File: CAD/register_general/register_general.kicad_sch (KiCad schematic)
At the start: 29 parts, among them J1 Conn_01x16_Pin, J2 Conn_01x16_Pin, J3 load select, J4 output select, U1 74HC245, U2 74HC377

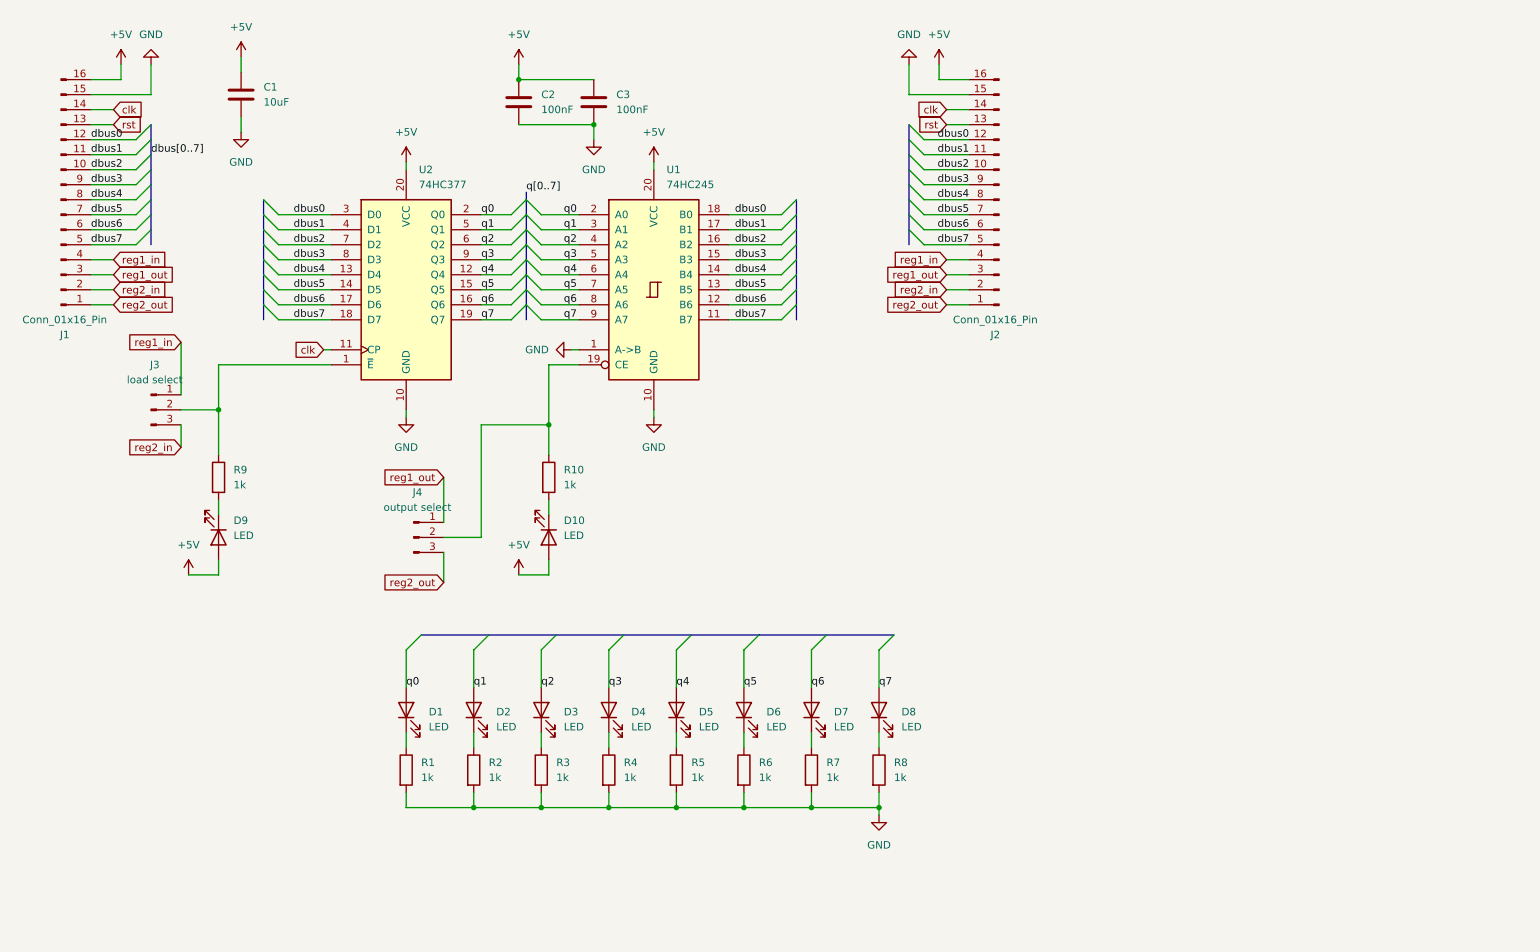
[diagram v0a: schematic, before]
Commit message: add NetClasses, TestPads, remove jumper pins
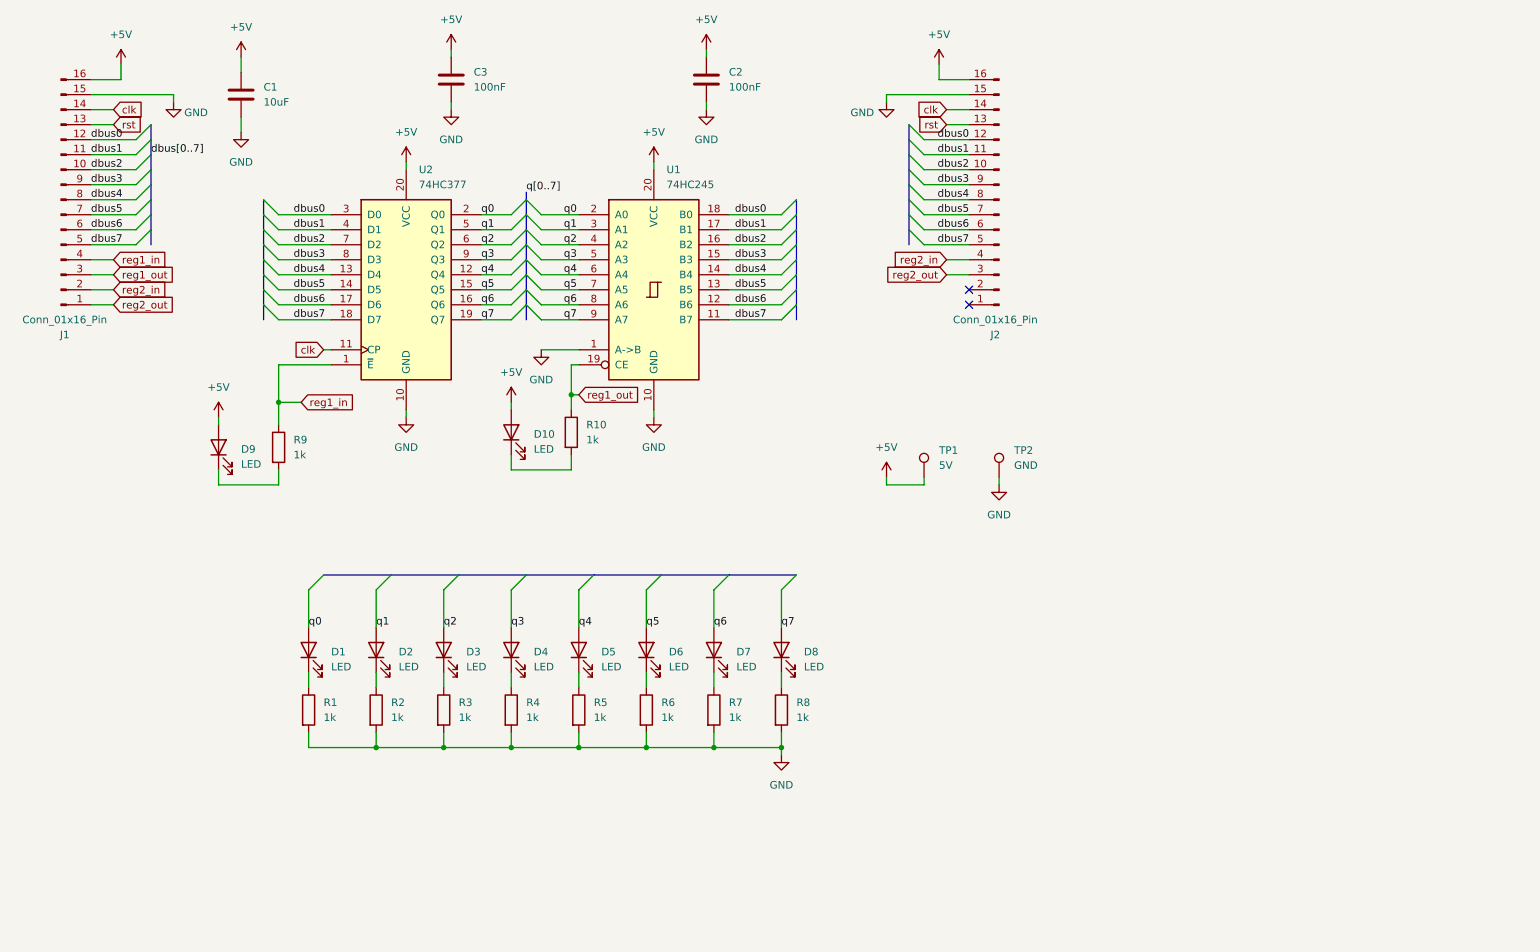
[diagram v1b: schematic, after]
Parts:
- removed J3: load select, Connector_PinHeader_2.54mm:PinHeader_1x03_P2.54mm_Vertical, symbol Connector:Conn_01x03_Pin
- removed J4: output select, Connector_PinHeader_2.54mm:PinHeader_1x03_P2.54mm_Vertical, symbol Connector:Conn_01x03_Pin
- added TP1: 5V, TestPoint:TestPoint_THTPad_D1.0mm_Drill0.5mm, symbol Connector:TestPoint
- added TP2: GND, TestPoint:TestPoint_THTPad_D1.0mm_Drill0.5mm, symbol Connector:TestPoint
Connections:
- net +5V: now also TP1.1
- net GND: now also TP2.1
- net reg1_in: now also R9.1, U2.1 (~{E}); no longer J2.4 (Pin_4)
- net reg1_out: now also R10.1, U1.19 (CE); no longer J2.3 (Pin_3)
- net reg2_in: now also J2.4 (Pin_4); no longer J2.2 (Pin_2)
- net reg2_out: now also J2.3 (Pin_3); no longer J2.1 (Pin_1)
- no-connect marks 0 -> 2
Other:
- moved on the sheet: C2, C3, D1, D10, D2, D3, D4, D5, D6, D7, D8, D9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

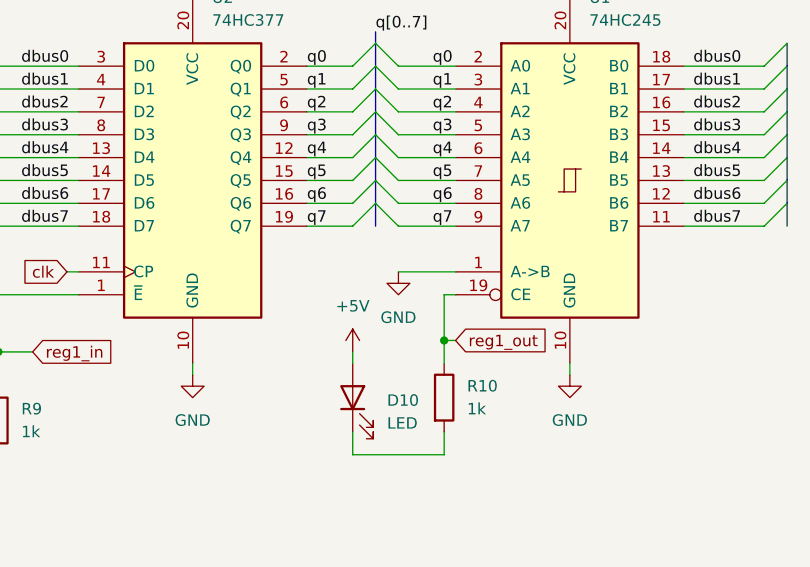
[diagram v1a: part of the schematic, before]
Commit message: fix HC245 dir signal
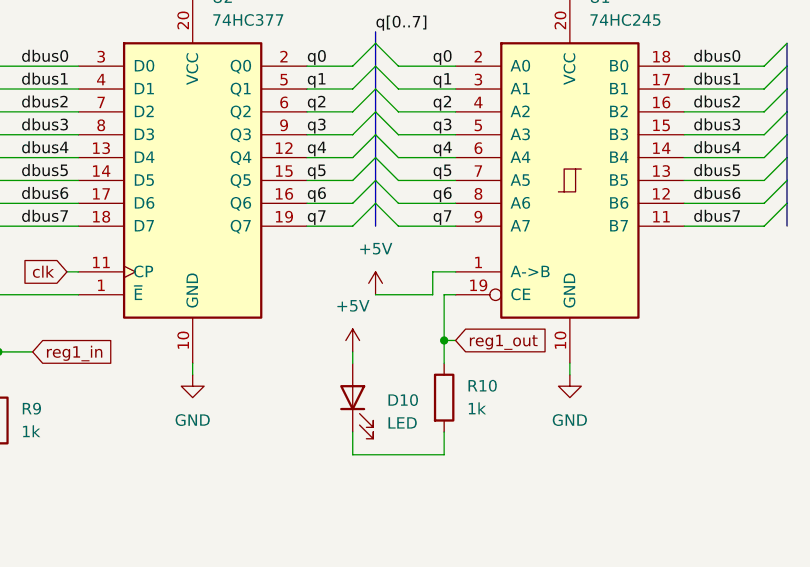
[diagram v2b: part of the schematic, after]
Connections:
- net +5V: now also U1.1 (A->B)
- net GND: no longer U1.1 (A->B)
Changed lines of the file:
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@@
 	(wire
 		(pts
+			(xy 115.57 80.01) (xy 118.11 80.01)
+		)
+		(stroke
+			(width 0)
+			(type default)
+		)
+	)
+	(wire
+		(pts
 			(xy 189.23 101.6) (xy 189.23 102.87)
 		)
@@
 	(wire
 		(pts
-			(xy 111.76 80.01) (xy 118.11 80.01)
+			(xy 109.22 82.55) (xy 115.57 82.55)
+		)
+		(stroke
+			(width 0)
+			(type default)
+		)
+	)
+	(wire
+		(pts
+			(xy 115.57 82.55) (xy 115.57 80.01)
 		)
 		(stroke
@@
 	)
 	(symbol
+		(lib_id "power:+5V")
+		(at 109.22 82.55 0)
+		(unit 1)
+		(exclude_from_sim no)
+		(in_bom yes)
+		(on_board yes)
+		(dnp no)
+		(fields_autoplaced yes)
+		(property "Reference" "#PWR07"
+			(at 109.22 86.36 0)
+			(effects
+				(font
+					(size 1.27 1.27)
+				)
+				(hide yes)
+			)
+		)
+		(property "Value" "+5V"
+			(at 109.22 77.47 0)
+			(effects
+				(font
+					(size 1.27 1.27)
+				)
+			)
+		)
+		(property "Footprint" ""
+			(at 109.22 82.55 0)
+			(effects
+				(font
+					(size 1.27 1.27)
+				)
+				(hide yes)
+			)
+		)
+		(property "Datasheet" ""
+			(at 109.22 82.55 0)
+			(effects
+				(font
+					(size 1.27 1.27)
+				)
+				(hide yes)
+			)
+		)
+		(property "Description" "Power symbol creates a global label with name \"+5V\""
+			(at 109.22 82.55 0)
+			(effects
+				(font
+					(size 1.27 1.27)
+				)
+				(hide yes)
+			)
+		)
+		(pin "1"
+		)
+		(instances
+			(project "register_general"
+				(path "/0d96e788-3788-4603-be87-fd7748d71811"
+					(reference "#PWR07")
+					(unit 1)
+				)
+			)
+		)
+	)
+	(symbol
 		(lib_id "Device:LED")
 		(at 72.39 130.81 90)
@@
 					(unit 1)
 				)
-			)
-		)
-	)
-	(symbol
-		(lib_id "power:GND")
-		(at 111.76 80.01 0)
-		(unit 1)
-		(exclude_from_sim no)
-		(in_bom yes)
-		(on_board yes)
-		(dnp no)
-		(fields_autoplaced yes)
-		(property "Reference" "#PWR07"
-			(at 111.76 86.36 0)
-			(effects
-				(font
-					(size 1.27 1.27)
-				)
-				(hide yes)
-			)
-		)
-		(property "Value" "GND"
-			(at 111.76 85.09 0)
-			(effects
-				(font
-					(size 1.27 1.27)
-				)
-			)
-		)
-		(property "Footprint" ""
-			(at 111.76 80.01 0)
-			(effects
-				(font
-					(size 1.27 1.27)
-				)
-				(hide yes)
-			)
-		)
-		(property "Datasheet" ""
-			(at 111.76 80.01 0)
-			(effects
-				(font
-					(size 1.27 1.27)
-				)
-				(hide yes)
-			)
-		)
-		(property "Description" "Power symbol creates a global label with name \"GND\" , ground"
-			(at 111.76 80.01 0)
-			(effects
-				(font
-					(size 1.27 1.27)
-				)
-				(hide yes)
-			)
-		)
-		(pin "1"
-		)
-		(instances
-			(project "register_general"
-				(path "/0d96e788-3788-4603-be87-fd7748d71811"
-					(reference "#PWR07")
-					(unit 1)
-				)

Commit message: add text variables for revision, etc.
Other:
- title: (none) -> General Purpose Register
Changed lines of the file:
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@@
 	(generator_version "9.0")
 	(paper "A4")
+	(title_block
+		(title "General Purpose Register")
+		(date "${YEAR}-${MONTH}-${DAY}")
+		(rev "${REVISION}")
+	)
 	(junction
 		(at 116.84 87.63)

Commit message: fix variables
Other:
- title: General Purpose Register -> ${TITLE}
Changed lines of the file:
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@@
 	(paper "A4")
 	(title_block
-		(title "General Purpose Register")
+		(title "${TITLE}")
 		(date "${YEAR}-${MONTH}-${DAY}")
 		(rev "${REVISION}")

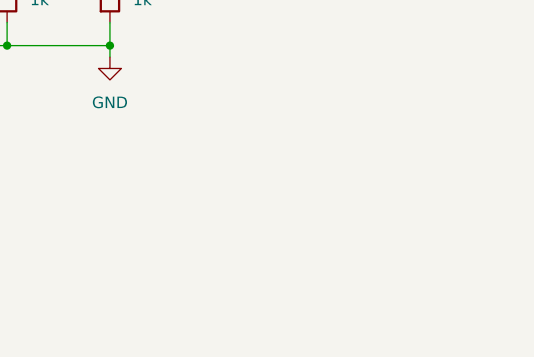
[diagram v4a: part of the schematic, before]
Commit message: update silkscreen qr code, license, add images
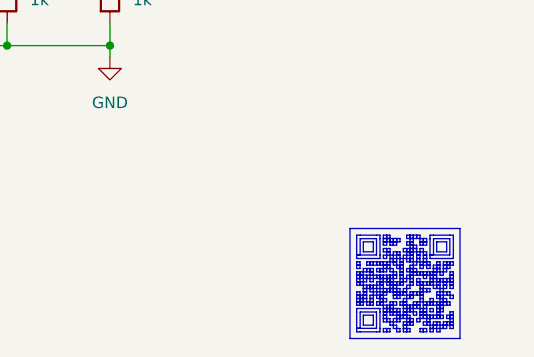
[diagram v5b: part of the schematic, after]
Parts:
- U1: symbol 74xx:74HC245 -> 8bit_computer:74HC245; Details (none) -> https://www.lcsc.com/product-detail/C88578.html; LCSC (none) -> C88578
- U2: Details (none) -> https://www.lcsc.com/product-detail/C7647.html; LCSC (none) -> C7647

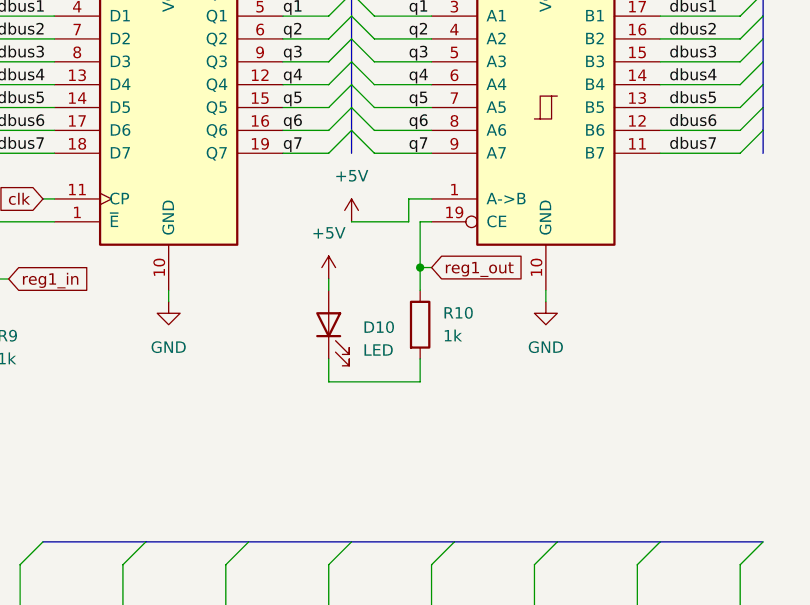
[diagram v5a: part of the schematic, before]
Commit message: add pull-up resistor to general register
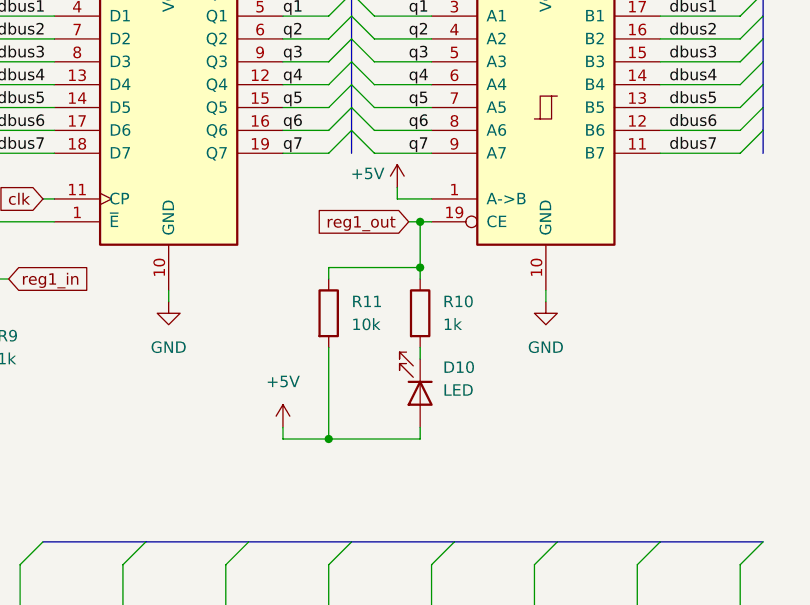
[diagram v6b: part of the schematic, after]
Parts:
- added R11: 10k, Resistor_SMD:R_0805_2012Metric, symbol Device:R
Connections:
- net +5V: now also R11.2
- net reg1_out: now also R11.1
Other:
- moved on the sheet: D10, R10
